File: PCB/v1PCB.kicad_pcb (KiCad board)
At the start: 2 copper layers, 369.9 x 125.4 mm, 223 parts, among them SW1 SW_PUSH, SW2 SW_PUSH, U1 STM32F072CBUx, U2 MCP1700-3302E_SOT23

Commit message: Nearing final production
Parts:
- F1: footprint Fuse:Fuse_1206_3216Metric -> Fuse:Fuse_0603_1608Metric
- moved R2 12.1 mm to (119.5, 181.5)
- moved SW2 11.9 mm to (117.0, 175.5)
- moved SW1 11.2 mm to (117.0, 168.7)
- moved R1 10.5 mm to (119.0, 162.8)
- moved C5 10.2 mm to (116.8, 107.4)
- moved R3 10.2 mm to (116.8, 109.2)
- moved C7 2.71 mm to (304.6, 208.6), turned to 180 degrees
- moved R4 1.99 mm to (131.1, 109.3)
- moved F1 1.98 mm to (126.5, 107.8)
- moved C3 1.59 mm to (304.1, 209.9), turned to 180 degrees
- moved C6 1.30 mm to (299.0, 220.8)
- moved C2 0.79 mm to (295.0, 211.5)
- moved C8 0.76 mm to (299.5, 219.5)
- moved C1 0.59 mm to (296.3, 211.8)
- moved R5 0.51 mm to (137.0, 109.3)
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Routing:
- net GND: track 452.4 -> 383.4 mm, vias 12 -> 7
- net BOOT0: track 208.2 -> 228.2 mm
- net Net-(C5-Pad2): track 24.1 -> 35.6 mm
- net col0: track 291.3 -> 283.9 mm
- net NRST: track 234.5 -> 239.8 mm
- net D-: track 319.7 -> 315.1 mm
- net D+: track 317.8 -> 313.2 mm
- net +3V3: track 340.2 -> 336.5 mm, vias 6 -> 7
- net col10: track 129.6 -> 131.9 mm, vias 0 -> 1
- net Net-(R4-Pad2): track 5.62 -> 3.47 mm
- net +5V: track 48.6 -> 50.6 mm
- net col8: track 141.6 -> 139.8 mm
- net col9: track 117.6 -> 118.5 mm
- net col5: track 185.1 -> 184.5 mm
- net Net-(R5-Pad2): track 2.68 -> 3.18 mm
- removed copper zone on B.Cu, net GND
- removed copper zone on F.Cu, net GND
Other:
- board size 369.9 x 125.4 mm -> 367.5 x 124.7 mm

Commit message: Final CAD models and PCB's are almost ready
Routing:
- net NRST: track 239.8 -> 240.8 mm
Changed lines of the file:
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@@
     (thickness 1.6)
     (drawings 27)
-    (tracks 1443)
+    (tracks 1445)
     (zones 0)
     (modules 223)
@@
   (segment (start 377.19 132.842) (end 377.19 168.56075) (width 0.254) (layer F.Cu) (net 15))
   (segment (start 377.19 168.56075) (end 374.80875 170.942) (width 0.254) (layer F.Cu) (net 15))
-  (segment (start 367.665 113.792) (end 367.665 123.317) (width 0.254) (layer F.Cu) (net 15))
-  (segment (start 367.665 123.317) (end 377.19 132.842) (width 0.254) (layer F.Cu) (net 15))
   (via (at 367.538 215.265) (size 0.8) (drill 0.4) (layers F.Cu B.Cu) (net 15))
   (segment (start 367.665 209.042) (end 367.665 215.138) (width 0.254) (layer F.Cu) (net 15))
@@
   (segment (start 309.734156 212.753) (end 313.325166 216.344011) (width 0.254) (layer B.Cu) (net 15))
   (segment (start 304.364 212.753) (end 309.734156 212.753) (width 0.254) (layer B.Cu) (net 15))
+  (segment (start 367.665 113.792) (end 367.665 119.634) (width 0.254) (layer F.Cu) (net 15))
+  (segment (start 367.665 119.634) (end 377.19 129.159) (width 0.254) (layer F.Cu) (net 15))
+  (segment (start 377.19 129.159) (end 377.19 132.842) (width 0.254) (layer F.Cu) (net 15))
   (segment (start 386.715 189.992) (end 386.715 209.042) (width 0.254) (layer F.Cu) (net 16))
   (segment (start 381.9525 151.892) (end 383.077499 153.016999) (width 0.254) (layer F.Cu) (net 16))
@@
   (segment (start 474.98 160.908) (end 474.98 163.322) (width 0.254) (layer B.Cu) (net 97))
   (segment (start 474.98 163.322) (end 471.805 166.497) (width 0.254) (layer B.Cu) (net 97))
-  (segment (start 155.067 190.178) (end 155.067 190.882) (width 0.254) (layer B.Cu) (net 98))
-  (segment (start 152.341 187.452) (end 155.067 190.178) (width 0.254) (layer B.Cu) (net 98))
-  (segment (start 138.27125 187.452) (end 152.341 187.452) (width 0.254) (layer B.Cu) (net 98))
+  (segment (start 141.70125 190.882) (end 155.067 190.882) (width 0.254) (layer B.Cu) (net 98))
+  (segment (start 138.27125 187.452) (end 141.70125 190.882) (width 0.254) (layer B.Cu) (net 98))
   (segment (start 169.2275 187.452) (end 171.9865 187.452) (width 0.254) (layer B.Cu) (net 99))
   (segment (start 171.9865 187.452) (end 175.2125 190.678) (width 0.254) (layer B.Cu) (net 99))
@@
   (segment (start 293.751 217.551) (end 298.196 221.996) (width 0.3048) (layer F.Cu) (net 129))
   (segment (start 293.751 211.385685) (end 293.751 210.82) (width 0.3048) (layer F.Cu) (net 129))
-  (segment (start 293.751 212.187554) (end 293.751 211.385685) (width 0.3048) (layer F.Cu) (net 129))
-  (segment (start 289.914744 216.02381) (end 293.751 212.187554) (width 0.3048) (layer F.Cu) (net 129))
   (segment (start 264.623098 216.02381) (end 289.914744 216.02381) (width 0.3048) (layer F.Cu) (net 129))
   (segment (start 292.22381 216.02381) (end 298.196 221.996) (width 0.3048) (layer F.Cu) (net 129))
@@
   (segment (start 308.16541 218.47954) (end 304.64895 221.996) (width 0.3048) (layer F.Cu) (net 129))
   (segment (start 304.64895 221.996) (end 302.895 221.996) (width 0.3048) (layer F.Cu) (net 129))
+  (segment (start 293.751 214.49662) (end 293.751 210.82) (width 0.3048) (layer F.Cu) (net 129))
+  (segment (start 292.22381 216.02381) (end 293.751 214.49662) (width 0.3048) (layer F.Cu) (net 129))
   (segment (start 113.717 166.406) (end 116.3715 163.7515) (width 0.254) (layer B.Cu) (net 130))
   (segment (start 117.2995 163.7515) (end 118.999 163.7515) (width 0.254) (layer B.Cu) (net 130))
   (segment (start 116.3715 163.7515) (end 117.2995 163.7515) (width 0.254) (layer B.Cu) (net 130))
-  (segment (start 121.4905 165.863538) (end 121.4905 191.222434) (width 0.254) (layer B.Cu) (net 130))
-  (segment (start 121.4905 191.222434) (end 127.045056 196.77699) (width 0.254) (layer B.Cu) (net 130))
   (via (at 301.713849 220.611751) (size 0.8) (drill 0.4) (layers F.Cu B.Cu) (net 130))
   (segment (start 300.6765 217.9405) (end 300.6765 219.574402) (width 0.254) (layer B.Cu) (net 130))
@@
   (segment (start 301.713849 220.611751) (end 297.605501 220.611751) (width 0.254) (layer F.Cu) (net 130))
   (segment (start 297.605501 220.611751) (end 294.48125 217.4875) (width 0.254) (layer F.Cu) (net 130))
-  (segment (start 119.555237 164.307737) (end 118.999 163.7515) (width 0.254) (layer B.Cu) (net 130))
-  (segment (start 119.934699 164.307737) (end 119.555237 164.307737) (width 0.254) (layer B.Cu) (net 130))
-  (segment (start 121.4905 165.863538) (end 119.934699 164.307737) (width 0.254) (layer B.Cu) (net 130))
   (segment (start 294.48125 217.4875) (end 294.48125 204.05725) (width 0.254) (layer F.Cu) (net 130))
   (via (at 288.72499 196.504) (size 0.8) (drill 0.4) (layers F.Cu B.Cu) (net 130))
   (segment (start 294.48125 204.05725) (end 288.72499 198.30099) (width 0.254) (layer F.Cu) (net 130))
   (segment (start 288.72499 198.30099) (end 288.72499 196.504) (width 0.254) (layer F.Cu) (net 130))
-  (segment (start 287.886315 196.77699) (end 286.07701 196.77699) (width 0.254) (layer B.Cu) (net 130))
-  (segment (start 288.159305 196.504) (end 287.886315 196.77699) (width 0.254) (layer B.Cu) (net 130))
+  (segment (start 121.92 179.705) (end 121.92 165.8725) (width 0.254) (layer B.Cu) (net 130))
+  (segment (start 120.98802 180.63698) (end 121.92 179.705) (width 0.254) (layer B.Cu) (net 130))
+  (segment (start 120.98802 190.71102) (end 120.98802 180.63698) (width 0.254) (layer B.Cu) (net 130))
+  (segment (start 119.799 163.7515) (end 118.999 163.7515) (width 0.254) (layer B.Cu) (net 130))
+  (segment (start 121.92 165.8725) (end 119.799 163.7515) (width 0.254) (layer B.Cu) (net 130))
   (segment (start 288.72499 196.504) (end 288.159305 196.504) (width 0.254) (layer B.Cu) (net 130))
-  (segment (start 127.045056 196.77699) (end 286.07701 196.77699) (width 0.254) (layer B.Cu) (net 130))
+  (segment (start 288.159305 196.504) (end 287.886315 196.77699) (width 0.254) (layer B.Cu) (net 130))
+  (segment (start 287.886315 196.77699) (end 127.045056 196.77699) (width 0.254) (layer B.Cu) (net 130))
+  (segment (start 127.045056 196.77699) (end 121.4905 191.222434) (width 0.254) (layer B.Cu) (net 130))
+  (segment (start 121.4905 191.222434) (end 121.4905 191.2135) (width 0.254) (layer B.Cu) (net 130))
+  (segment (start 121.4905 191.2135) (end 120.98802 190.71102) (width 0.254) (layer B.Cu) (net 130))
   (segment (start 119.507 178.474) (end 120.217 177.764) (width 0.254) (layer B.Cu) (net 131))
   (segment (start 119.507 180.5455) (end 119.507 178.474) (width 0.254) (layer B.Cu) (net 131))

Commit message: Updates
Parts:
- moved R5 1.11 mm to (136.9, 110.5)
- moved R4 1.08 mm to (131.3, 110.4)
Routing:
- net D+: track 313.2 -> 382.1 mm
- net D-: track 315.1 -> 277.0 mm
- net +3V3: track 336.1 -> 329.7 mm
- net col9: track 118.5 -> 116.6 mm
- net GND: track 383.4 -> 385.2 mm
- net Net-(R5-Pad2): track 3.18 -> 4.23 mm
- net Net-(R4-Pad2): track 3.47 -> 4.42 mm
- added copper zone on B.Cu, net GND
- added copper zone on F.Cu, net GND
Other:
- board size 367.5 x 124.7 mm -> 367.5 x 123 mm
- board text added: "BOOT0"
- board text added: "FUNCTION96"
- board text added: "ML JTM V1.1"
- board text added: "RESET"
- board text added: "Thank you for making my project reality!"
- board text removed: "ML JTM V1"

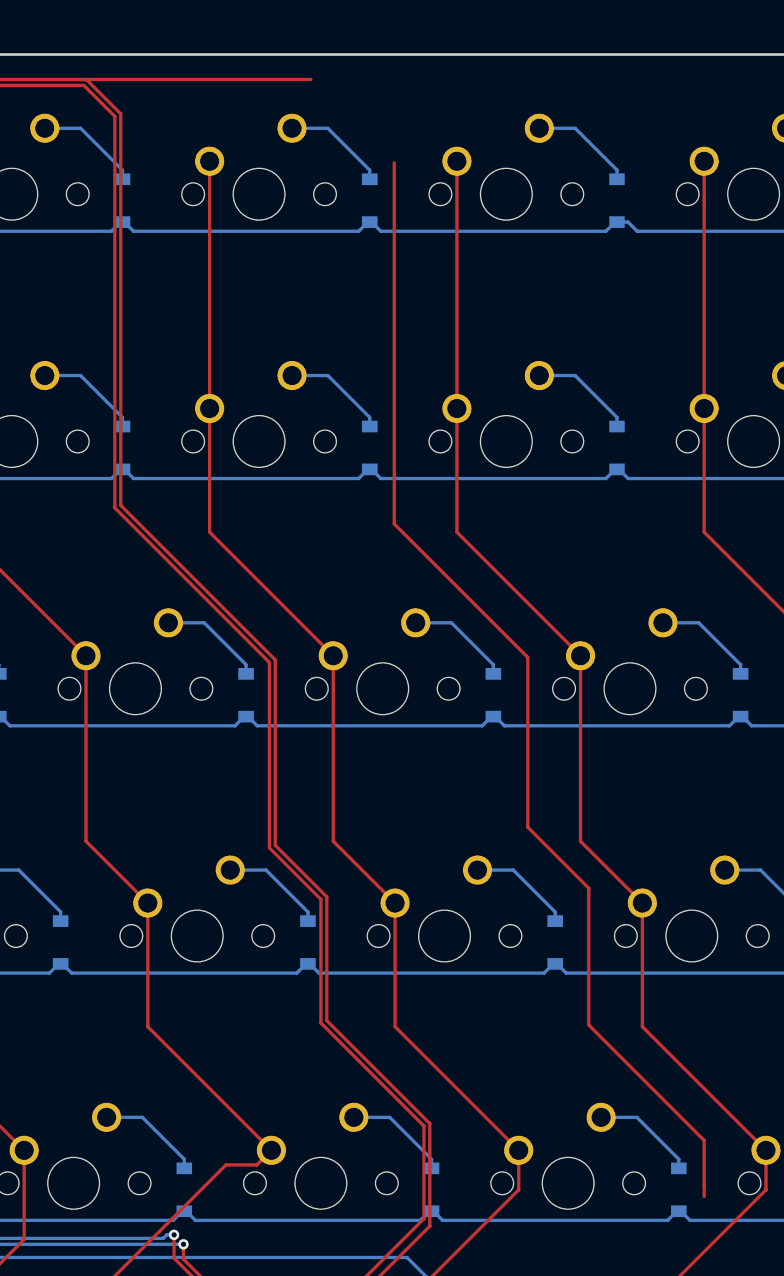
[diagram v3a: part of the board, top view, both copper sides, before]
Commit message: Updates to PCB and CAD. Incorrect PaP files, beware EasyEDA
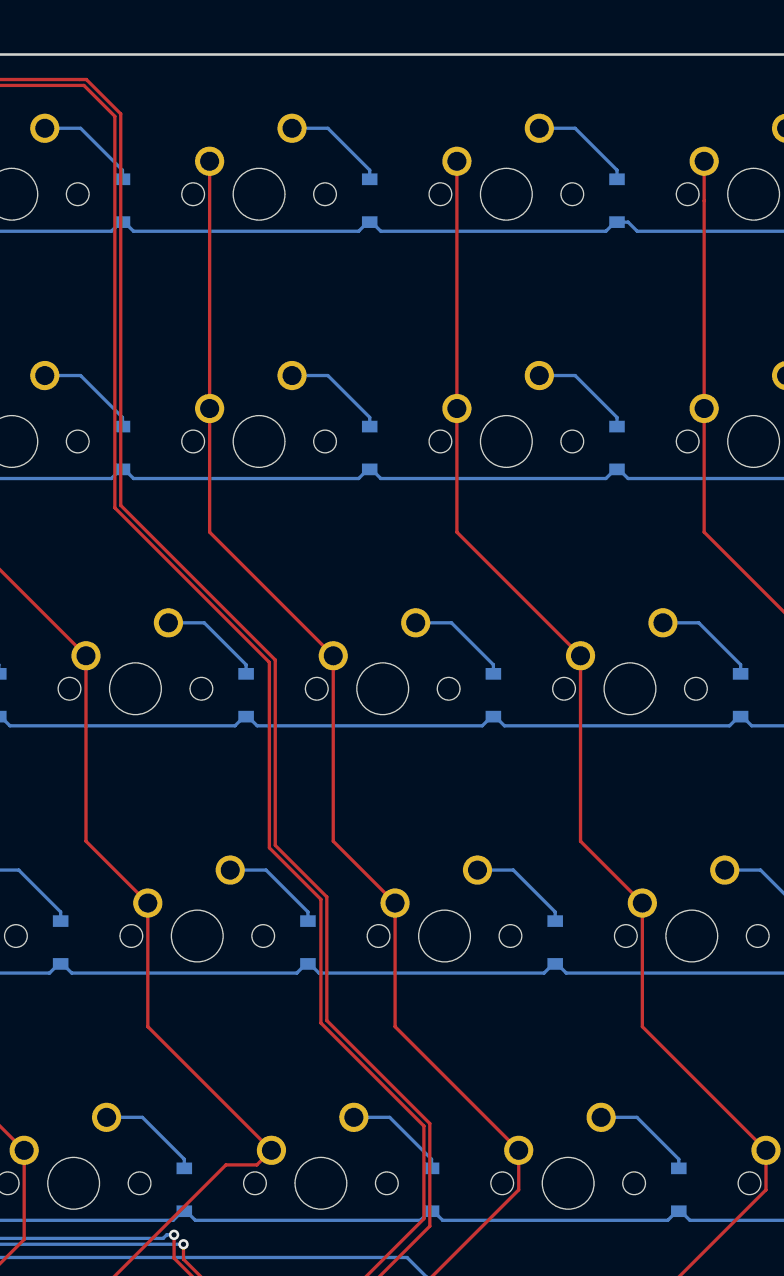
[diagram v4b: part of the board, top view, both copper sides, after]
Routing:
- net D+: track 382.1 -> 274.7 mm
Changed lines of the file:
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@@
-(kicad_pcb (version 20171130) (host pcbnew "(5.1.6)-1")
+(kicad_pcb (version 20171130) (host pcbnew "(5.1.4)-1")
   (general
     (thickness 1.6)
     (drawings 25)
-    (tracks 1440)
+    (tracks 1431)
     (zones 0)
     (modules 223)
@@
     (pcbplotparams
       (layerselection 0x010f0_ffffffff)
-      (usegerberextensions true)
+      (usegerberextensions false)
       (usegerberattributes false)
       (usegerberadvancedattributes false)
@@
   (segment (start 134.366 107.569) (end 134.62 107.569) (width 0.254) (layer B.Cu) (net 132))
   (segment (start 134.23675 107.569) (end 134.366 107.569) (width 0.254) (layer B.Cu) (net 132))
-  (segment (start 329.565 192.7225) (end 329.565 193.548) (width 0.254) (layer F.Cu) (net 132))
-  (segment (start 329.565 189.23) (end 329.565 192.7225) (width 0.254) (layer F.Cu) (net 132))
-  (segment (start 320.675 180.34) (end 329.565 189.23) (width 0.254) (layer F.Cu) (net 132))
-  (segment (start 320.675 169.799) (end 320.675 180.34) (width 0.254) (layer F.Cu) (net 132))
-  (segment (start 315.976 152.019) (end 315.976 165.1) (width 0.254) (layer F.Cu) (net 132))
-  (segment (start 305.689 141.732) (end 315.976 152.019) (width 0.254) (layer F.Cu) (net 132))
-  (segment (start 305.689 113.919) (end 305.689 141.732) (width 0.254) (layer F.Cu) (net 132))
-  (segment (start 315.976 165.1) (end 320.675 169.799) (width 0.254) (layer F.Cu) (net 132))
   (segment (start 141.60323 108.26573) (end 141.603233 108.26573) (width 0.254) (layer F.Cu) (net 132))
   (segment (start 141.603233 108.26573) (end 142.372973 107.49599) (width 0.254) (layer F.Cu) (net 132))
@@
   (segment (start 281.969307 107.49599) (end 284.61651 110.143193) (width 0.254) (layer F.Cu) (net 132))
   (segment (start 281.44151 107.49599) (end 281.969307 107.49599) (width 0.254) (layer F.Cu) (net 132))
-  (segment (start 281.44151 107.49599) (end 299.265991 107.49599) (width 0.254) (layer F.Cu) (net 132))
   (segment (start 142.372973 107.49599) (end 281.44151 107.49599) (width 0.254) (layer F.Cu) (net 132))
   (segment (start 284.61651 110.143193) (end 284.61651 140.305694) (width 0.254) (layer F.Cu) (net 132))
